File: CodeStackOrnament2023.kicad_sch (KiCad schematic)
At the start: 21 parts, among them U1 4040, U2 NE555D

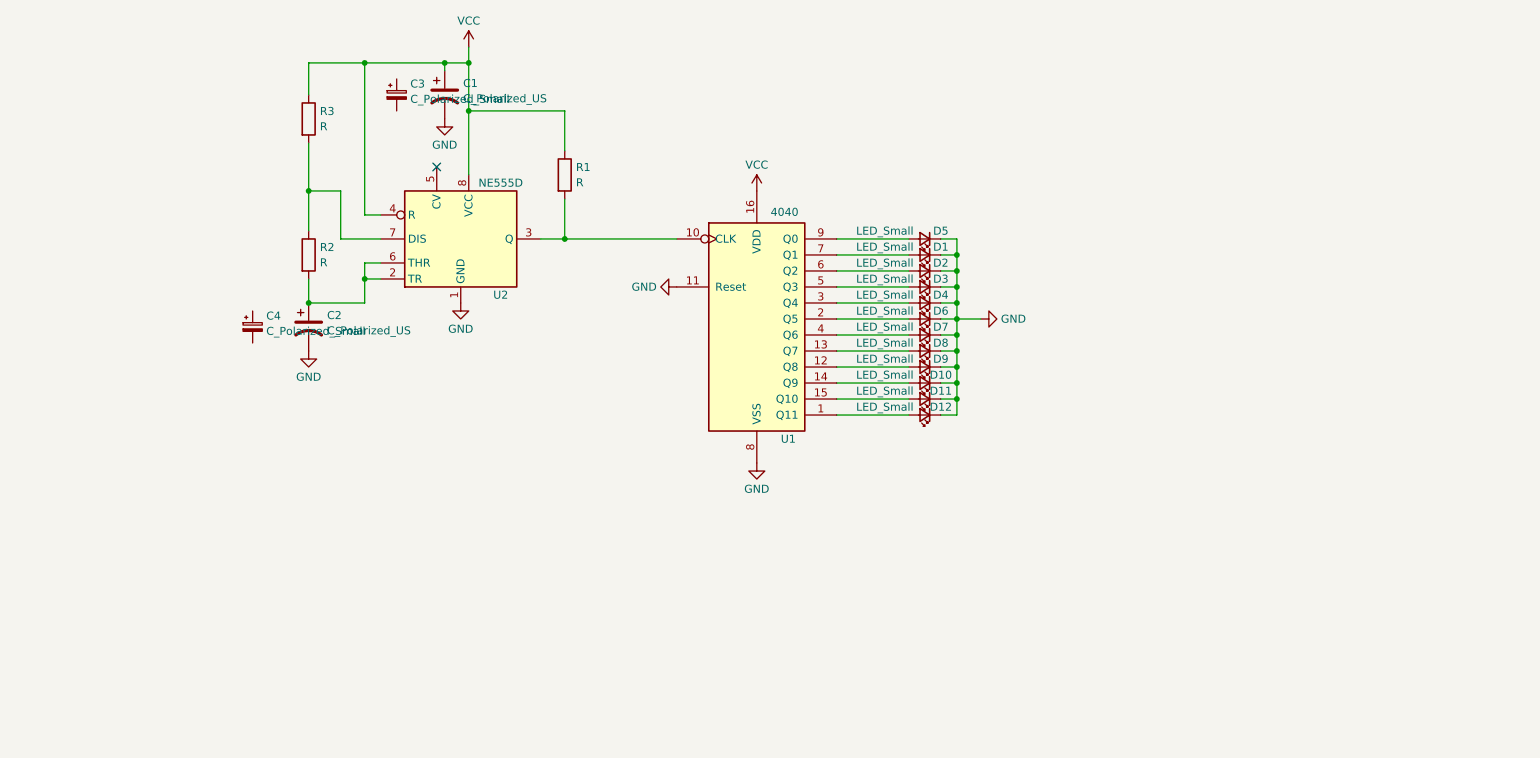
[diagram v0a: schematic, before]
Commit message: adding battery and boost circuit
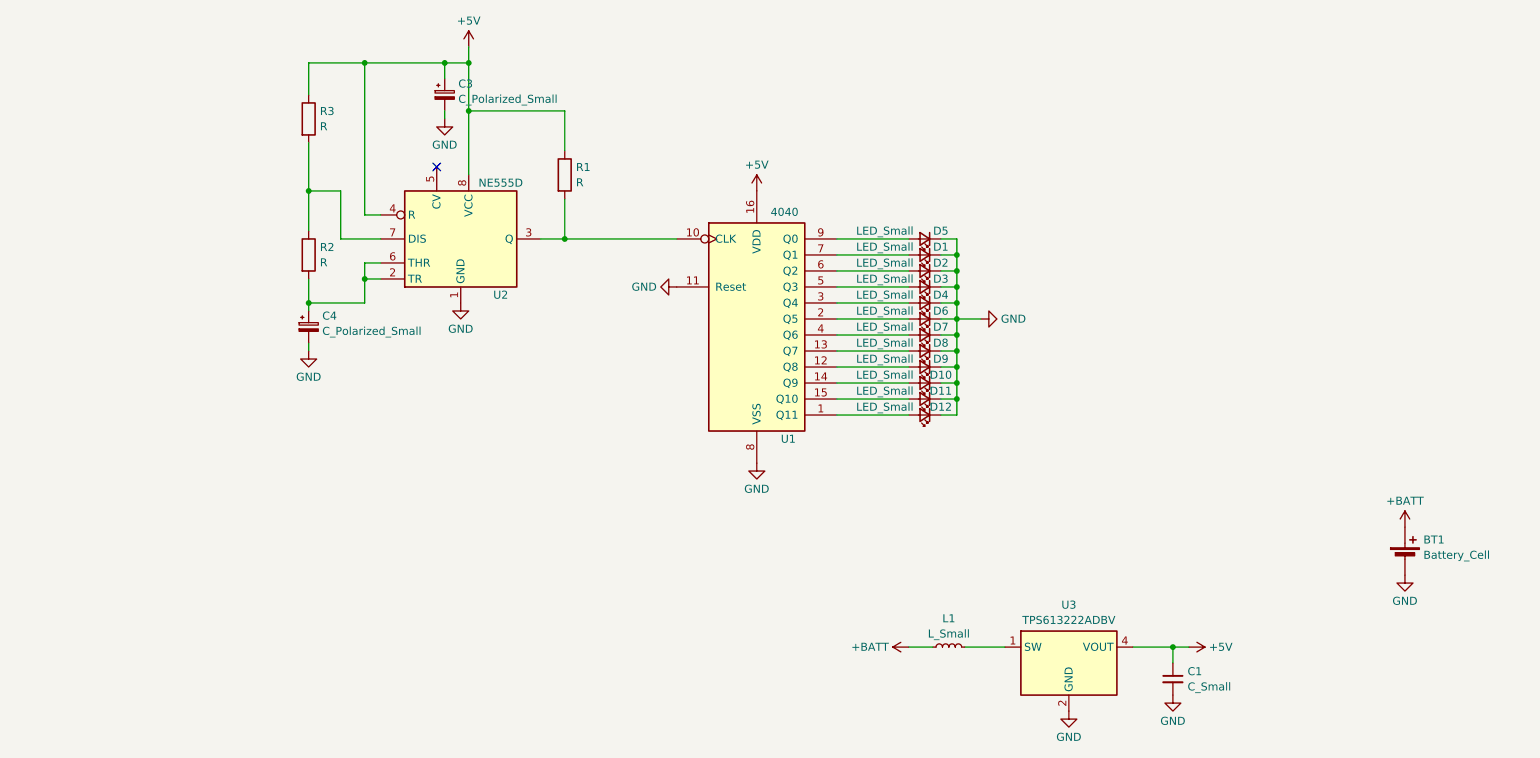
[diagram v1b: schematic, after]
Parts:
- removed C1, C2: C_Polarized_US, symbol Device:C_Polarized_US
- added BT1: Battery_Cell, symbol Device:Battery_Cell
- added C1: C_Small, symbol Device:C_Small
- added L1: L_Small, symbol Device:L_Small
- added U3: TPS613222ADBV, Package_TO_SOT_SMD:SOT-23-5, symbol Regulator_Switching:TPS613222ADBV
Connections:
- net VCC is gone; now on net +5V: R1.1, R3.1, U1.16 (VDD), U2.4 (R), U2.8 (VCC)
- net GND: now also C3.2, C4.2, BT1.2 (-), C1.2, U3.2 (GND)
- net at R2.2, U2.2 (TR), U2.6 (THR): now also C4.1
- net +5V: now reaches C3.1
- net +5V: now also C1.1, U3.4 (VOUT)
- new net: L1.2, U3.1 (SW)
- new net +BATT: BT1.1 (+), L1.1
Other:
- moved on the sheet: C3, C4

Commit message: finishing schematic. starting on footprints.
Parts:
- added SW1: SW_SPST, symbol Switch:SW_SPST
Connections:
- net +BATT: now also SW1.2 (B); no longer BT1.1 (+)
- new net: BT1.1 (+), SW1.1 (A)
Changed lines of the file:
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@@
   (junction (at 172.72 69.85) (diameter 0) (color 0 0 0 0)
+  )
+  (junction (at 177.8 116.84) (diameter 0) (color 0 0 0 0)
   )
   (junction (at 69.85 62.23) (diameter 0) (color 0 0 0 0)
@@
     (stroke (width 0) (type default))
   )
-  (wire (pts (xy 173.99 116.84) (xy 180.34 116.84))
+  (wire (pts (xy 173.99 116.84) (xy 177.8 116.84))
     (stroke (width 0) (type default))
   )
@@
   )
   (wire (pts (xy 153.67 80.01) (xy 165.1 80.01))
+    (stroke (width 0) (type default))
+  )
+  (wire (pts (xy 177.8 116.84) (xy 180.34 116.84))
     (stroke (width 0) (type default))
   )
@@
     )
   )
+  (symbol (lib_id "Switch:SW_SPST") (at 243.84 92.71 90) (unit 1)
+    (in_bom yes) (on_board yes) (dnp no) (fields_autoplaced)
+    (property "Reference" "SW1" (at 244.983 91.4979 90)
+      (effects (font (size 1.27 1.27)) (justify right))
+    )
+    (property "Value" "SW_SPST" (at 244.983 93.9221 90)
+      (effects (font (size 1.27 1.27)) (justify right))
+    )
+    (property "Footprint" "" (at 243.84 92.71 0)
+      (effects (font (size 1.27 1.27)) hide)
+    )
+    (property "Datasheet" "~" (at 243.84 92.71 0)
+      (effects (font (size 1.27 1.27)) hide)
+    )
+    (pin "1")
+    (pin "2")
+    (instances
+      (project "CodeStackOrnament2023"
+        (path "/42e733f2-c99f-4cc2-86e2-d5b5a803e3a0"
+          (reference "SW1") (unit 1)
+        )
+      )
+    )
+  )
   (symbol (lib_id "CodeStackOrnament2023Library:NE555D") (at 93.98 52.07 0) (unit 1)
     (in_bom yes) (on_board yes) (dnp no)
@@
     )
   )
+  (symbol (lib_id "power:+BATT") (at 220.98 88.9 180) (unit 1)
+    (in_bom yes) (on_board yes) (dnp no) (fields_autoplaced)
+    (property "Reference" "#PWR05" (at 220.98 85.09 0)
+      (effects (font (size 1.27 1.27)) hide)
+    )
+    (property "Value" "+BATT" (at 220.98 93.0331 0)
+      (effects (font (size 1.27 1.27)))
+    )
+    (property "Footprint" "" (at 220.98 88.9 0)
+      (effects (font (size 1.27 1.27)) hide)
+    )
+    (property "Datasheet" "" (at 220.98 88.9 0)
+      (effects (font (size 1.27 1.27)) hide)
+    )
+    (pin "1")
+    (instances
+      (project "CodeStackOrnament2023"
+        (path "/42e733f2-c99f-4cc2-86e2-d5b5a803e3a0"
+          (reference "#PWR05") (unit 1)
+        )
+      )
+    )
+  )
+  (symbol (lib_id "power:PWR_FLAG") (at 177.8 116.84 180) (unit 1)
+    (in_bom yes) (on_board yes) (dnp no) (fields_autoplaced)
+    (property "Reference" "#FLG03" (at 177.8 118.745 0)
+      (effects (font (size 1.27 1.27)) hide)
+    )
+    (property "Value" "PWR_FLAG" (at 177.8 120.9731 0)
+      (effects (font (size 1.27 1.27)))
+    )
+    (property "Footprint" "" (at 177.8 116.84 0)
+      (effects (font (size 1.27 1.27)) hide)
+    )
+    (property "Datasheet" "~" (at 177.8 116.84 0)
+      (effects (font (size 1.27 1.27)) hide)
+    )
+    (pin "1")
+    (instances
+      (project "CodeStackOrnament2023"
+        (path "/42e733f2-c99f-4cc2-86e2-d5b5a803e3a0"
+          (reference "#FLG03") (unit 1)
+        )
+      )
+    )
+  )
   (symbol (lib_id "Device:Battery_Cell") (at 243.84 102.87 0) (unit 1)
     (in_bom yes) (on_board yes) (dnp no) (fields_autoplaced)
@@
         (path "/42e733f2-c99f-4cc2-86e2-d5b5a803e3a0"
           (reference "D11") (unit 1)
+        )
+      )
+    )
+  )
+  (symbol (lib_id "power:GND") (at 207.01 88.9 0) (unit 1)
+    (in_bom yes) (on_board yes) (dnp no) (fields_autoplaced)
+    (property "Reference" "#PWR04" (at 207.01 95.25 0)
+      (effects (font (size 1.27 1.27)) hide)
+    )
+    (property "Value" "GND" (at 207.01 93.0331 0)
+      (effects (font (size 1.27 1.27)))
+    )
+    (property "Footprint" "" (at 207.01 88.9 0)
+      (effects (font (size 1.27 1.27)) hide)
+    )
+    (property "Datasheet" "" (at 207.01 88.9 0)
+      (effects (font (size 1.27 1.27)) hide)
+    )
+    (pin "1")
+    (instances
+      (project "CodeStackOrnament2023"
+        (path "/42e733f2-c99f-4cc2-86e2-d5b5a803e3a0"
+          (reference "#PWR04") (unit 1)
         )
       )
@@
     )
   )
+  (symbol (lib_id "power:PWR_FLAG") (at 207.01 88.9 0) (unit 1)
+    (in_bom yes) (on_board yes) (dnp no) (fields_autoplaced)
+    (property "Reference" "#FLG01" (at 207.01 86.995 0)
+      (effects (font (size 1.27 1.27)) hide)
+    )
+    (property "Value" "PWR_FLAG" (at 207.01 84.7669 0)
+      (effects (font (size 1.27 1.27)))
+    )
+    (property "Footprint" "" (at 207.01 88.9 0)
+      (effects (font (size 1.27 1.27)) hide)
+    )
+    (property "Datasheet" "~" (at 207.01 88.9 0)
+      (effects (font (size 1.27 1.27)) hide)
+    )
+    (pin "1")
+    (instances
+      (project "CodeStackOrnament2023"
+        (path "/42e733f2-c99f-4cc2-86e2-d5b5a803e3a0"
+          (reference "#FLG01") (unit 1)
+        )
+      )
+    )
+  )
   (symbol (lib_id "power:+BATT") (at 165.1 116.84 90) (unit 1)
     (in_bom yes) (on_board yes) (dnp no) (fields_autoplaced)
@@
     )
   )
-  (symbol (lib_id "power:+BATT") (at 243.84 97.79 0) (unit 1)
-    (in_bom yes) (on_board yes) (dnp no) (fields_autoplaced)
-    (property "Reference" "#PWR09" (at 243.84 101.6 0)
-      (effects (font (size 1.27 1.27)) hide)
-    )
-    (property "Value" "+BATT" (at 243.84 93.6569 0)
-      (effects (font (size 1.27 1.27)))
-    )
-    (property "Footprint" "" (at 243.84 97.79 0)
-      (effects (font (size 1.27 1.27)) hide)
-    )
-    (property "Datasheet" "" (at 243.84 97.79 0)
+  (symbol (lib_id "power:+BATT") (at 243.84 87.63 0) (unit 1)
+    (in_bom yes) (on_board yes) (dnp no) (fields_autoplaced)
+    (property "Reference" "#PWR09" (at 243.84 91.44 0)
+      (effects (font (size 1.27 1.27)) hide)
+    )
+    (property "Value" "+BATT" (at 243.84 83.4969 0)
+      (effects (font (size 1.27 1.27)))
+    )
+    (property "Footprint" "" (at 243.84 87.63 0)
+      (effects (font (size 1.27 1.27)) hide)
+    )
+    (property "Datasheet" "" (at 243.84 87.63 0)
       (effects (font (size 1.27 1.27)) hide)
     )
@@
         )
       )
+    )
+  )
+  (symbol (lib_id "power:PWR_FLAG") (at 220.98 88.9 0) (unit 1)
+    (in_bom yes) (on_board yes) (dnp no) (fields_autoplaced)
+    (property "Reference" "#FLG02" (at 220.98 86.995 0)
+      (effects (font (size 1.27 1.27)) hide)
+    )
+    (property "Value" "PWR_FLAG" (at 220.98 84.7669 0)
+      (effects (font (size 1.27 1.27)))
+    )
+    (property "Footprint" "" (at 220.98 88.9 0)
+      (effects (font (size 1.27 1.27)) hide)
+    )
+    (property "Datasheet" "~" (at 220.98 88.9 0)
+      (effects (font (size 1.27 1.27)) hide)
+    )
+    (pin "1")
+    (instances
+      (project "CodeStackOrnament2023"
+        (path "/42e733f2-c99f-4cc2-86e2-d5b5a803e3a0"
+          (reference "#FLG02") (unit 1)
+        )
+      )

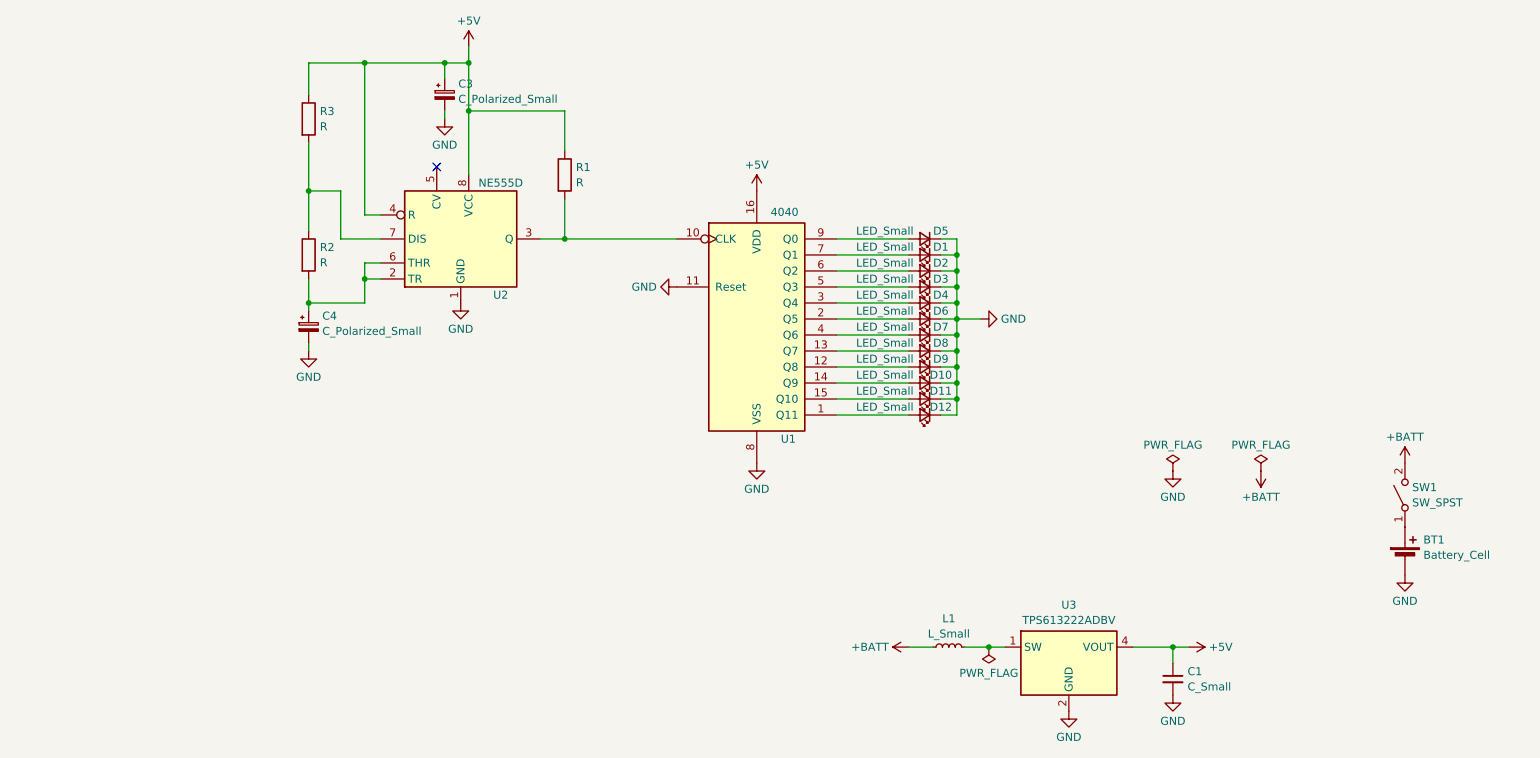
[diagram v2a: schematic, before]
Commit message: adding footprint for battery holder
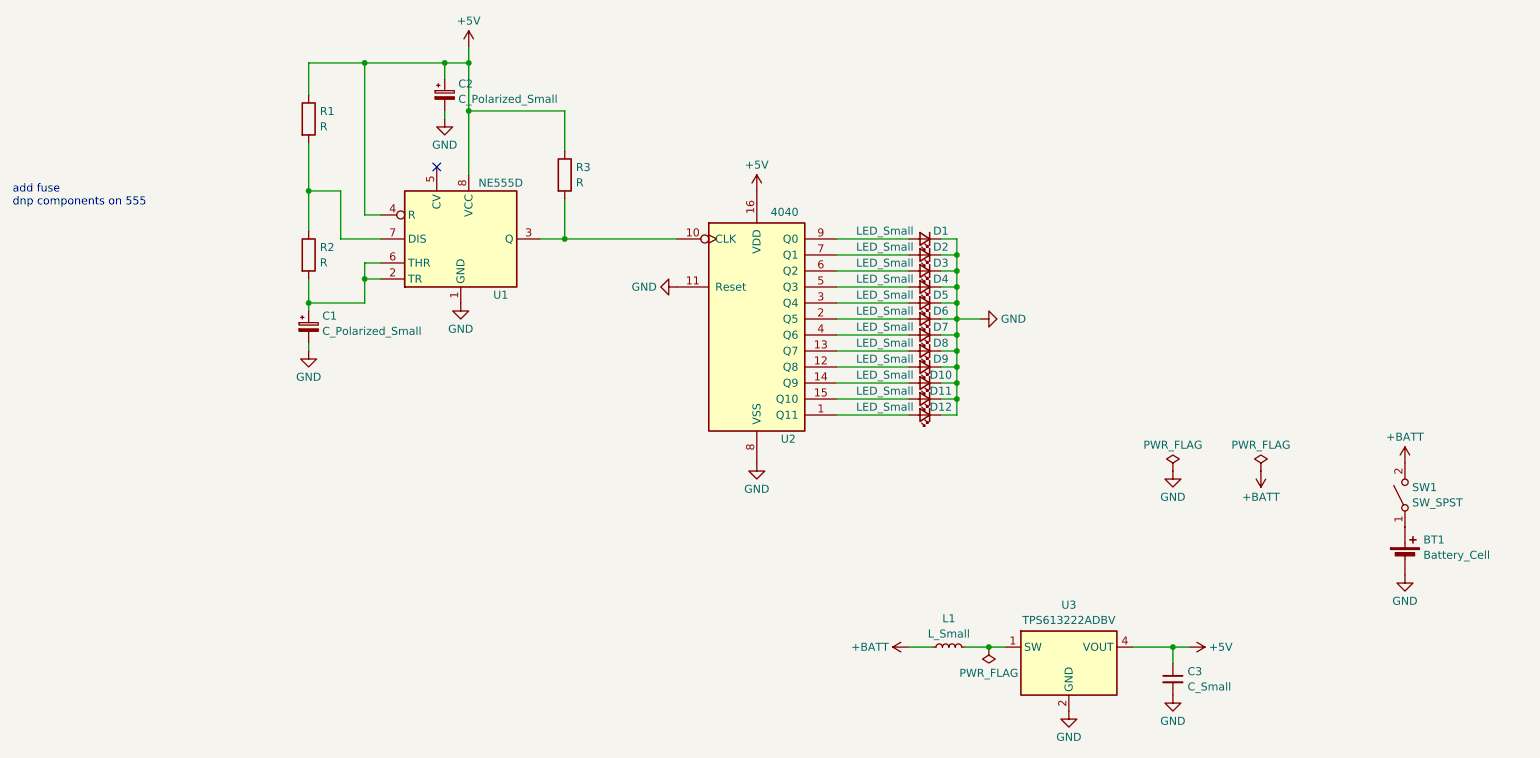
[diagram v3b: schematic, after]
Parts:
- C1: renamed from C4; footprint (none) -> Capacitor_SMD:C_0805_2012Metric
- C2: renamed from C3; footprint (none) -> Capacitor_SMD:C_0805_2012Metric
- C3: renamed from C1; footprint (none) -> Capacitor_SMD:C_0805_2012Metric
- D1: renamed from D5; footprint (none) -> CodeStackOrnament2023Footprints:156120RS75300_LED
- D10, D11, D12, D6, D7, D8, D9: footprint (none) -> CodeStackOrnament2023Footprints:156120RS75300_LED
- D2: renamed from D1; footprint (none) -> CodeStackOrnament2023Footprints:156120RS75300_LED
- D3: renamed from D2; footprint (none) -> CodeStackOrnament2023Footprints:156120RS75300_LED
- D4: renamed from D3; footprint (none) -> CodeStackOrnament2023Footprints:156120RS75300_LED
- D5: renamed from D4; footprint (none) -> CodeStackOrnament2023Footprints:156120RS75300_LED
- R1: renamed from R3; footprint (none) -> Resistor_SMD:R_0805_2012Metric
- R2: footprint (none) -> Resistor_SMD:R_0805_2012Metric
- R3: renamed from R1; footprint (none) -> Resistor_SMD:R_0805_2012Metric
- SW1: footprint (none) -> CodeStackOrnament2023Footprints:JS202011SCQN_SWITCH
- U2: renamed from U1; footprint (none) -> Package_SO:TSSOP-16_4.4x5mm_P0.65mm
- renumbered U2 to U1
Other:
- note added: "add fuse dnp components on 555"

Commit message: refactoring power
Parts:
- removed C3: C_Small, Capacitor_SMD:C_0805_2012Metric, symbol Device:C_Small
- removed L1: L_Small, symbol Device:L_Small
- removed U3: TPS613222ADBV, Package_TO_SOT_SMD:SOT-23-5, symbol Regulator_Switching:TPS613222ADBV
- added F1: Polyfuse_Small, symbol Device:Polyfuse_Small
- BT1: footprint (none) -> CodeStackOrnament2023Footprints:2466_AAA_HOLDER
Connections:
- net +5V renamed +3V0
- net +3V0: now also F1.1
- net +BATT: no longer names the net of SW1.2 (B)
- net +BATT: now also F1.2
